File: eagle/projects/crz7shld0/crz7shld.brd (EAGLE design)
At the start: 89 x 79 mm, 52 parts, among them IC1 IS62WV51216BLL-55T, J1 HDR-2X6, J2 HDR-2X6, J3 HDR-2X8, J4 HDR-2X3, J5 HDR-2X8, J6 HDR-2X6, J7 HDR-2X6, Q2 BSS138, Q3 BSS138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

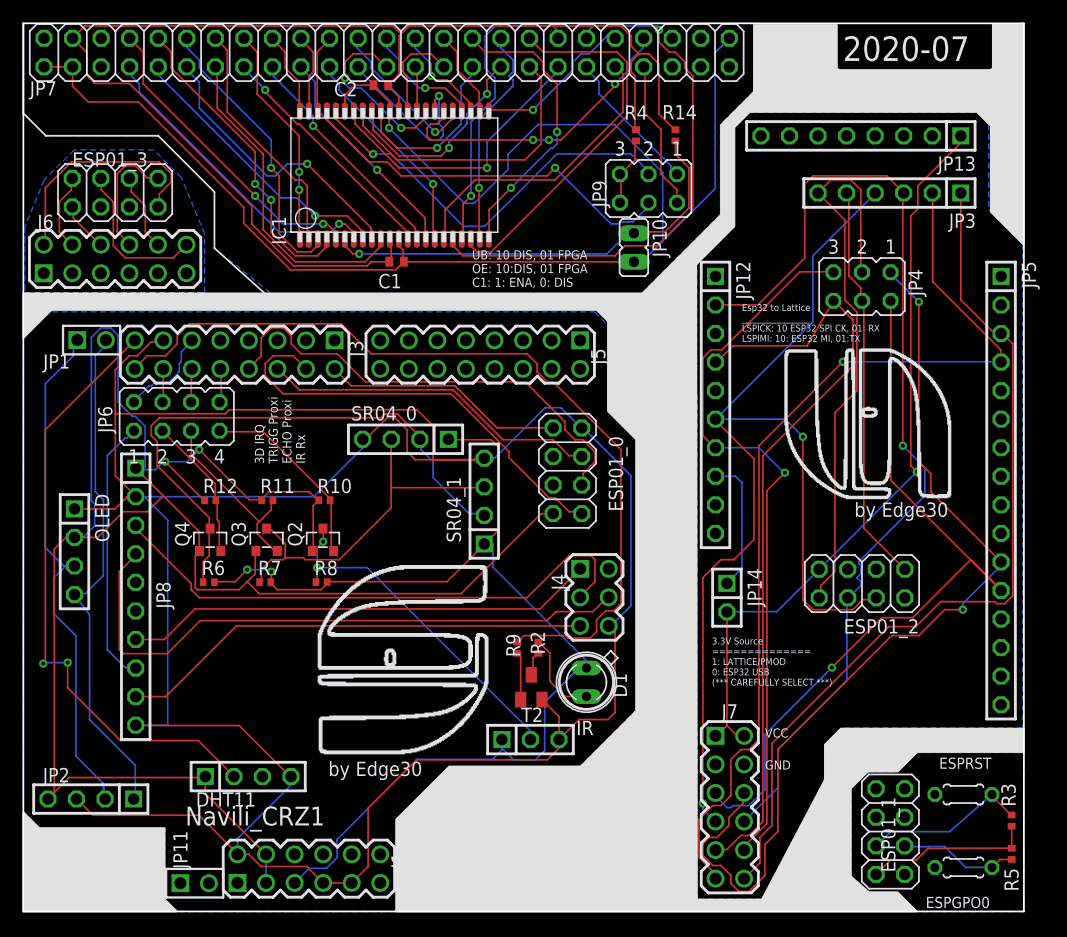
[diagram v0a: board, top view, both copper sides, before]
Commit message: order JLCPCB crz7shld1
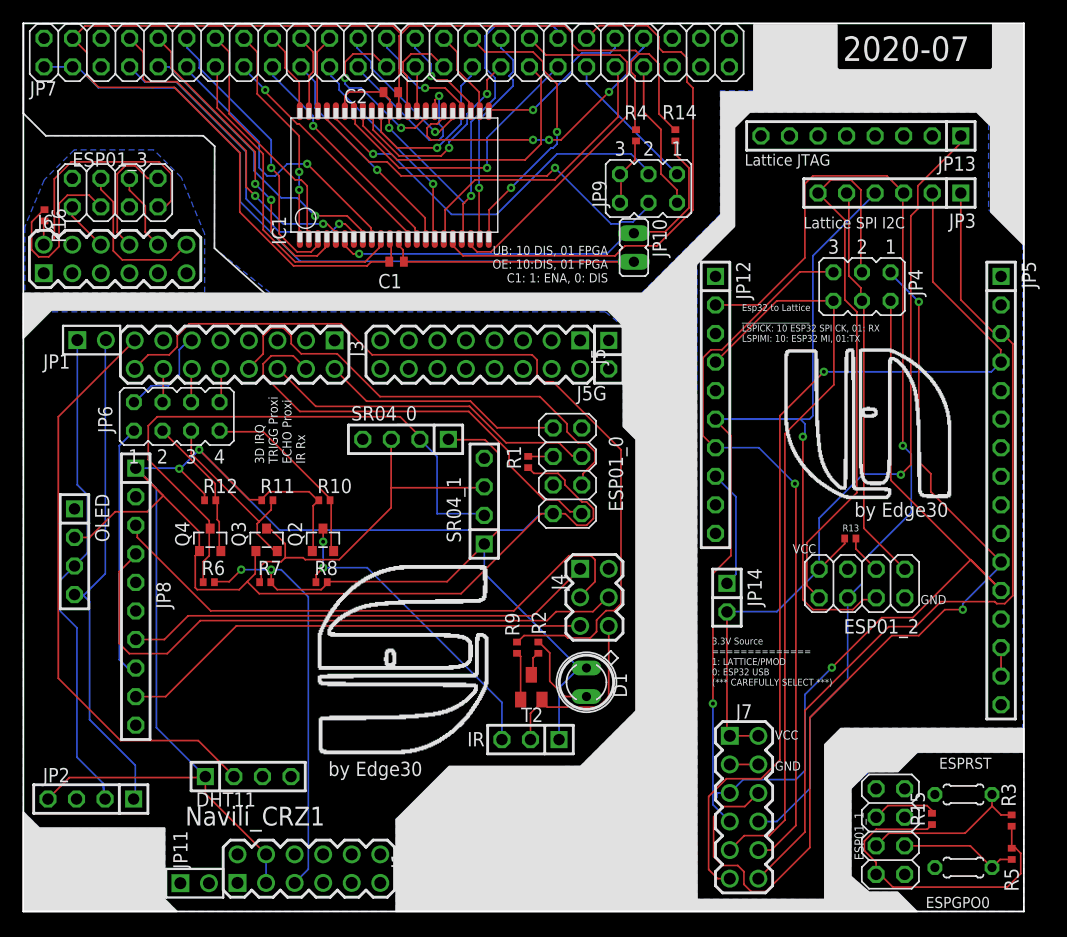
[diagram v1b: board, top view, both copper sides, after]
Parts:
- added J5G: (no value), pinhead2:1X02
- added R1, R13, R15, R16: 10k, rcl:R0402
- moved J7 1.27 mm to (64.1, 9.27)
- moved C2 1.09 mm to (32.7, 72.9)
- turned IR to 180 degrees
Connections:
- new net N$10: ESP01_3.3, R16.1
- new net N$6: ESP01_0.3, R1.2
- new net N$8: ESP01_2.3, R13.1
- new net N$9: ESP01_1.3, R15.2
- net GND: now also IR.2, J5G.1, J5G.2; no longer IR.3
- net IR_OUT: now also IR.3; no longer IR.2
- net VCC: now also R1.1
- net VCC2ND: now also R15.1
- net VCC3RD: now also R16.2
- net VCCLAT: now also R13.2
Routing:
- net GND: track 253.1 -> 18.1 mm
- net SRGND: track 136.8 -> 104.7 mm
- net VCC: track 177.8 -> 197.7 mm
- net N$10: track 0.00 -> 15.4 mm
- net VCC2ND: track 15.0 -> 28.6 mm
- net GND3RD: track 6.85 -> 0.00 mm
- net N$9: track 0.00 -> 5.83 mm
- net VCCLAT: track 67.4 -> 72.9 mm
- net GNDLAT: track 0.00 -> 5.08 mm
- net N$8: track 0.00 -> 3.48 mm
- net SCL: track 48.7 -> 45.3 mm
- net LSPIMO: track 96.5 -> 99.7 mm
- net VCC3RD: track 21.2 -> 23.8 mm
- net SENSIN: track 54.6 -> 52.1 mm, vias 2 -> 0
- net +5V: track 96.8 -> 94.5 mm
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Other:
- board text added: "Lattice JTAG"
- board text added: "Lattice SPI I2C"
- board text added: "PMOD"
